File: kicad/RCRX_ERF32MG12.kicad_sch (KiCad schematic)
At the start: 79 parts, among them J21 BUZZER, J22 USB_OTG, P1 Nokia 5110 display, Q1 Q_PMOS_DGS, SW1 RESET, U1 PIC16(L)F1459-I_ML

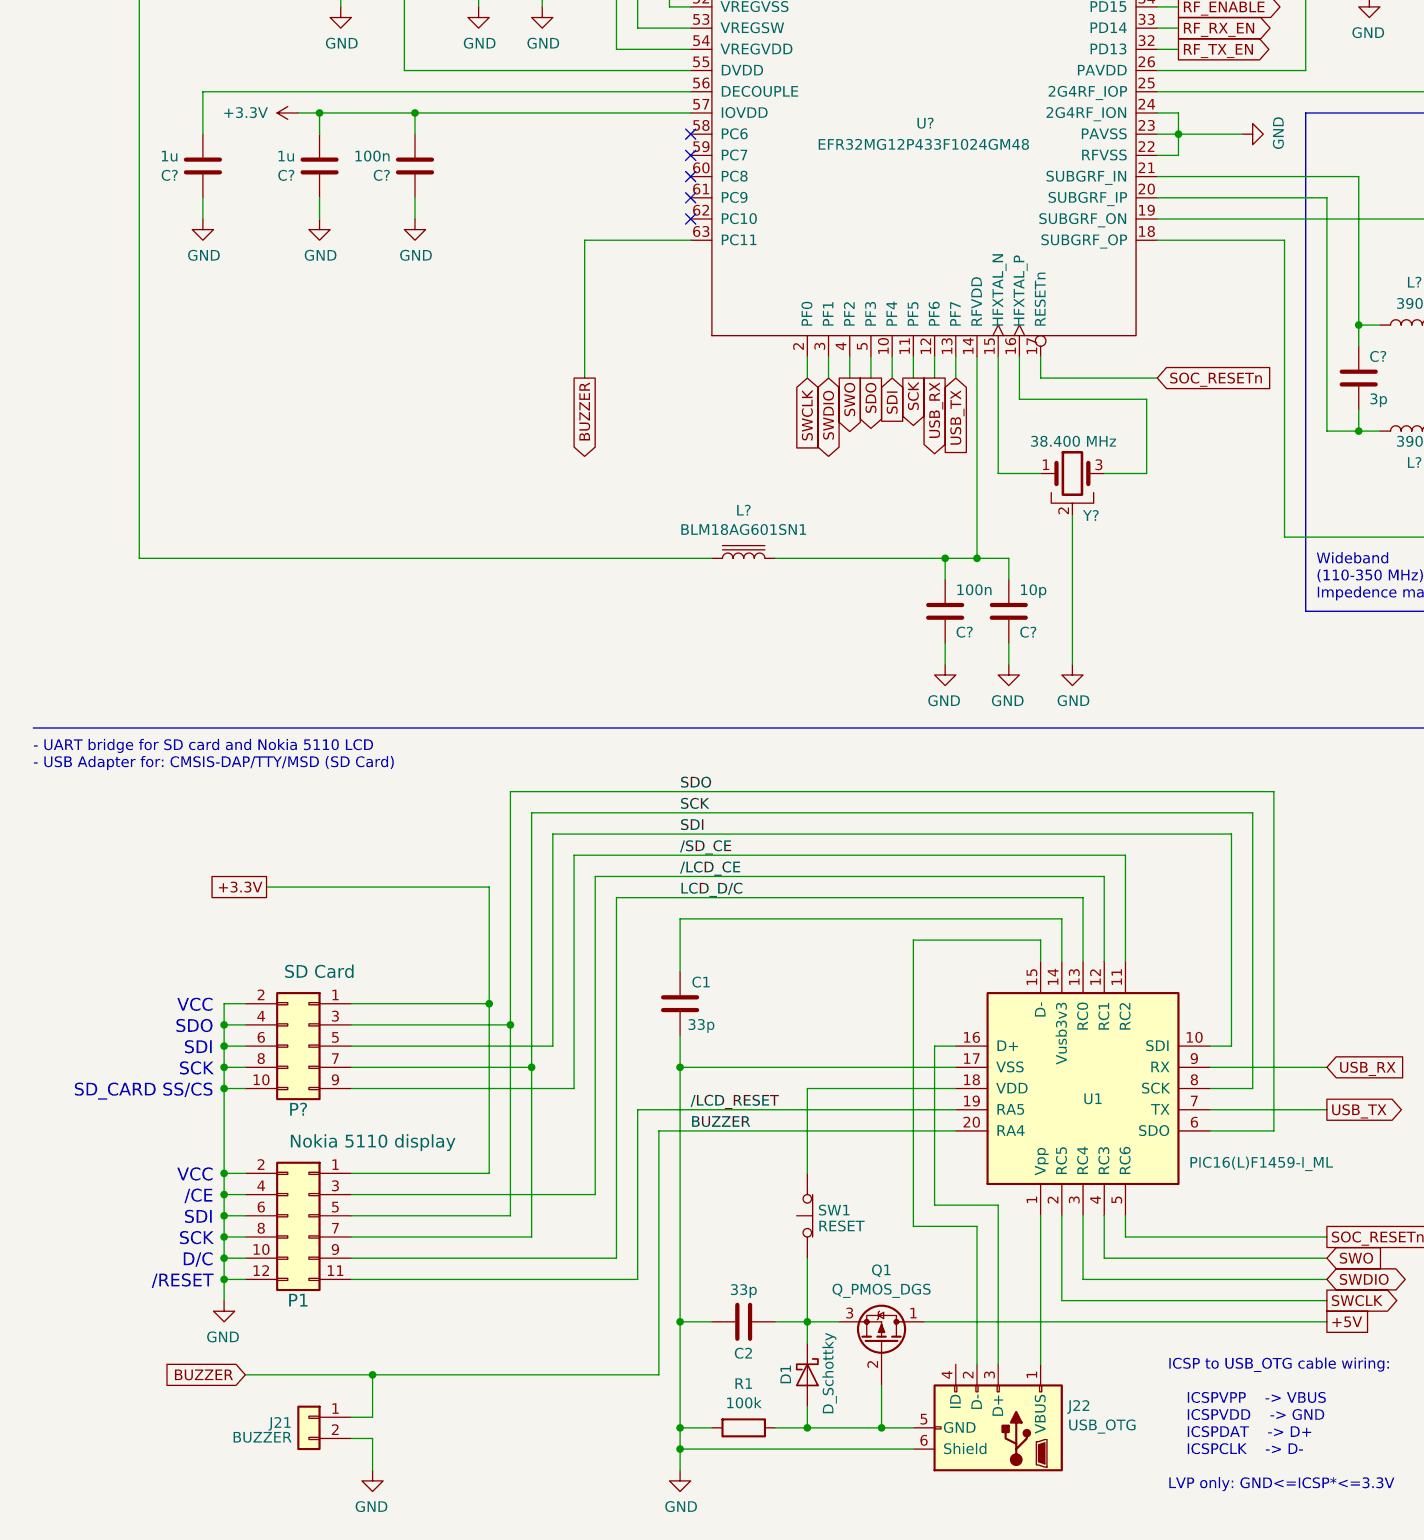
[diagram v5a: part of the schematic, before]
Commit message: Changing the buzzer connector
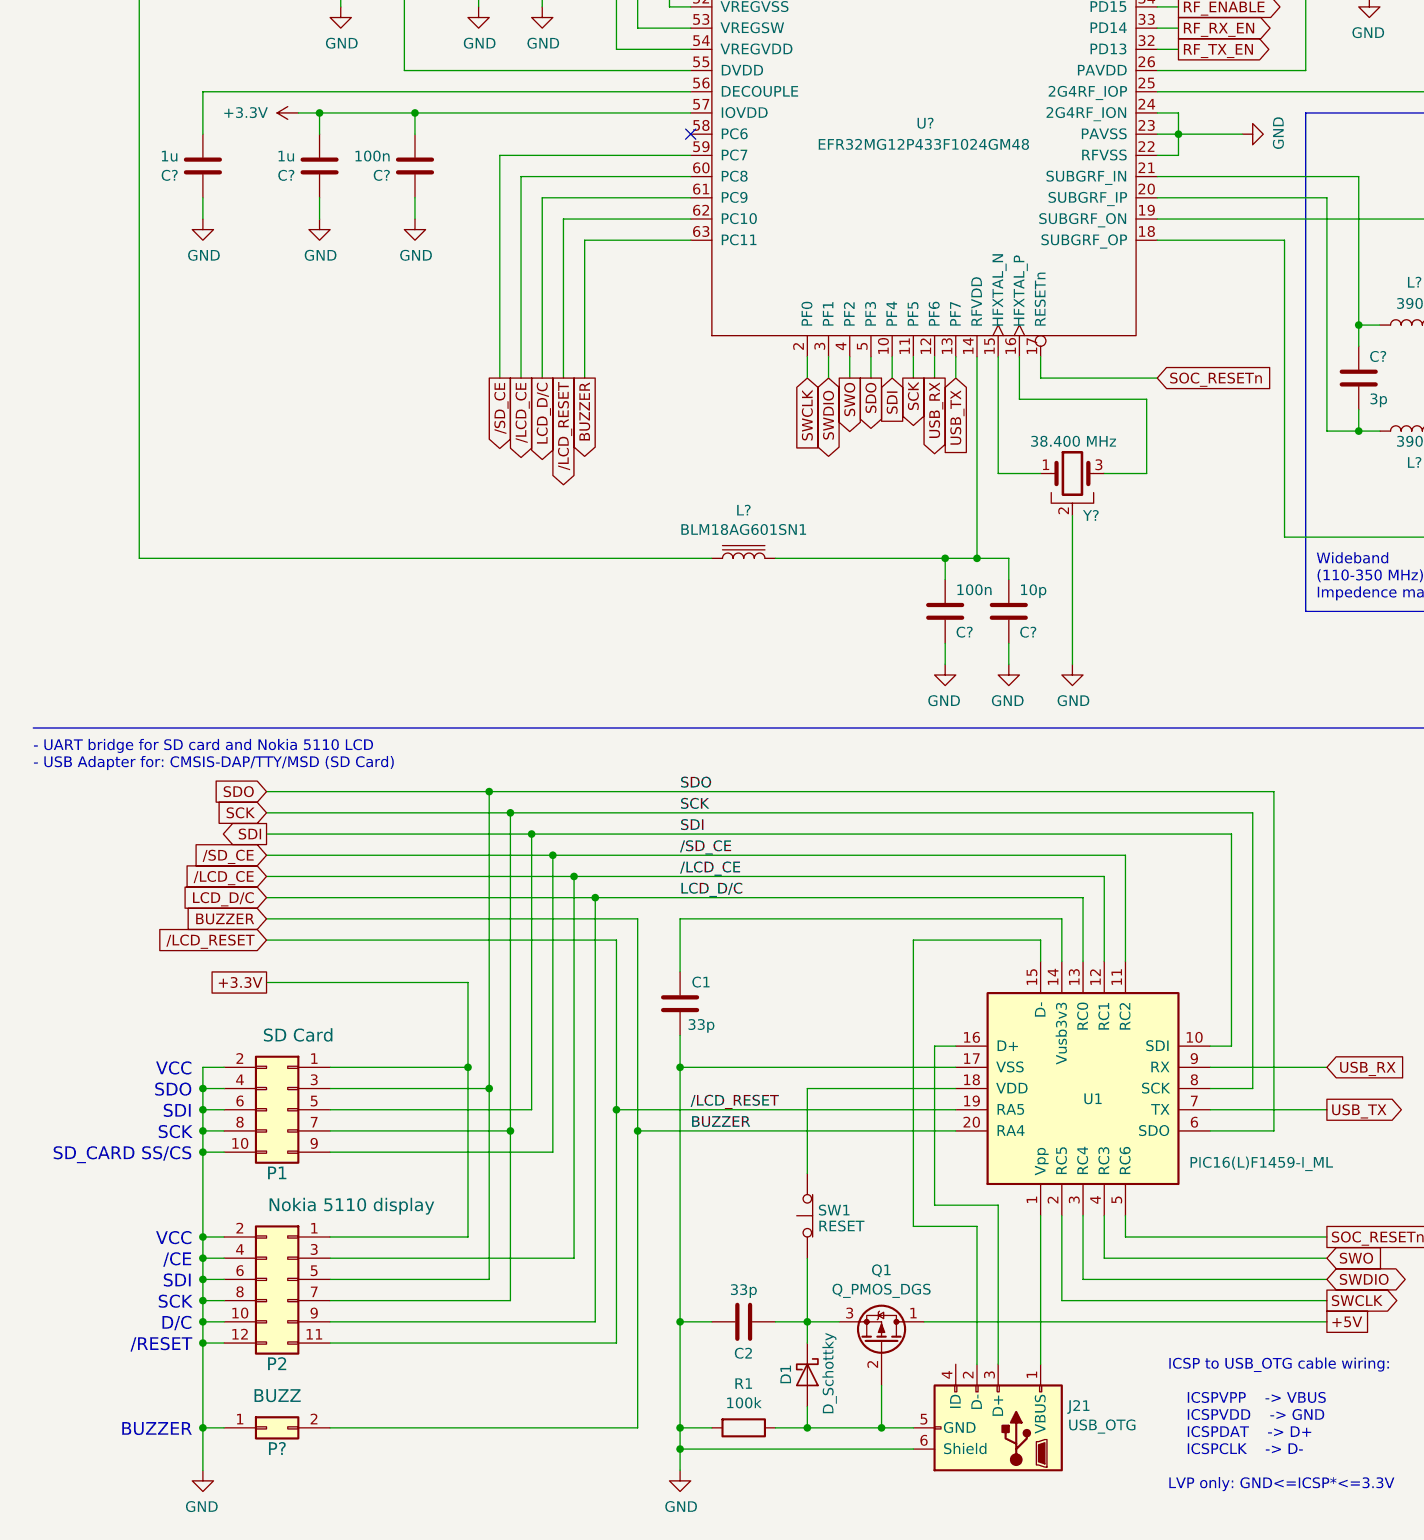
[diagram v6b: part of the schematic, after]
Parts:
- removed J21: BUZZER, symbol Connector_Generic:Conn_01x02
- removed J22: USB_OTG, symbol conn:USB_OTG
- removed P1: Nokia 5110 display, symbol conn:Conn_02x06_Odd_Even
- removed P?: SD Card, symbol conn:Conn_02x05_Odd_Even
- added J21: USB_OTG, symbol conn:USB_OTG
- added P1: SD Card, symbol conn:Conn_02x05_Odd_Even
- added P2: Nokia 5110 display, symbol conn:Conn_02x06_Odd_Even
- added P?: BUZZ, symbol conn:Conn_02x01
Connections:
- net +3V3: now also P1.1 (Pin_1), P2.1 (Pin_1)
- net BUZZER: now also P?.2 (Pin_2)
- net GND: now also J21.6 (Shield), P1.10 (Pin_10), P1.2 (Pin_2), P1.4 (Pin_4), P1.6 (Pin_6), P1.8 (Pin_8), P2.10 (Pin_10), P2.12 (Pin_12), P2.2 (Pin_2), P2.4 (Pin_4), P2.6 (Pin_6), P2.8 (Pin_8), P?.1 (Pin_1)
- net LCD_D/C: now also U?.61 (PC9), P2.9 (Pin_9)
- net SCK: now also P1.7 (Pin_7), P2.7 (Pin_7)
- net SDI: now also P1.5 (Pin_5)
- net SDO: now also P1.3 (Pin_3), P2.5 (Pin_5)
- net /LCD_CE: now also U?.60 (PC8), P2.3 (Pin_3)
- net /LCD_RESET: now also U?.62 (PC10), P2.11 (Pin_11)
- net /SD_CE: now also U?.59 (PC7), P1.9 (Pin_9)
- net at D1.2 (A), Q1.2 (G), R1.1: now also J21.5 (GND)
- net at U1.1 (Vpp): now also J21.1 (VBUS)
- net at U1.15 (D-): now also J21.2 (D-)
- net at U1.16 (D+): now also J21.3 (D+)
- no-connect marks 8 -> 4
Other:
- note added: "BUZZER"

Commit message: Using SAMD11D14M instead of PIC16F1459 for USB bridge - updating schematics
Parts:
- removed C1, C2: 33p, symbol device:C
- removed D1: D_Schottky, symbol device:D_Schottky
- removed J21: USB_OTG, symbol conn:USB_OTG
- removed P1: SD Card, symbol conn:Conn_02x05_Odd_Even
- removed P2: Nokia 5110 display, symbol conn:Conn_02x06_Odd_Even
- removed P?: BUZZ, symbol conn:Conn_02x01
- removed Q1: Q_PMOS_DGS, symbol device:Q_PMOS_DGS
- removed R1: 100k, symbol device:R
- removed SW1: RESET, symbol switches:SW_Push_Open
- removed U1: PIC16(L)F1459-I_ML, symbol PIC_USB_BRIDGE:PIC16(L)F1459-I_ML
- added C16: 100n, symbol device:C
- added C17, C19: 4.7u, symbol device:C
- added J20: USB_OTG, symbol conn:USB_OTG
- added J21, J22: USB, symbol Connector_Generic:Conn_01x03
- added P10: LEDs, symbol conn:Conn_02x06_Odd_Even
- added P6: SD Card, symbol conn:Conn_02x05_Odd_Even
- added P9: BUZZ, symbol conn:Conn_02x01
- added P?: DAP, symbol Connector_Generic:Conn_02x09_Odd_Even
- added P?: Nokia 5110 display, symbol Connector_Generic:Conn_02x07_Odd_Even
- added R10: 1M, symbol device:R
- added R7: 1k, symbol device:R
- added U10: ATSAMD11D14A-M, Package_DFN_QFN:QFN-24-1EP_4x4mm_P0.5mm_EP2.6x2.6mm, symbol MCU_Microchip_SAMD:ATSAMD11D14A-M
- added U11: USB6B1, Package_SO:SOIC-8_3.9x4.9mm_P1.27mm, symbol Power_Protection:USB6B1
- C?: value 100n -> 2.0pF
- C?: value 100n -> 1.0pF
- L?: value L -> 1.8nH
- L?: value L -> 3.0nH
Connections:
- net +3V3: now also C16.2, C17.2, P10.3 (Pin_3), P6.1 (Pin_1), P?.1 (Pin_1), P?.3 (Pin_3), R7.2, U10.24 (VDD)
- net +5V: now also P10.1 (Pin_1), P?.1 (Pin_1)
- net GND: now also C16.1, C17.1, C19.1, J20.5 (GND), J21.3 (Pin_3), J22.3 (Pin_3), P10.10 (Pin_10), P10.12 (Pin_12), P10.2 (Pin_2), P10.4 (Pin_4), P10.6 (Pin_6), P10.8 (Pin_8), P6.10 (Pin_10), P6.2 (Pin_2), P6.4 (Pin_4), P6.6 (Pin_6), P6.8 (Pin_8), P9.2 (Pin_2), P?.10 (Pin_10), P?.10 (Pin_10), P?.12 (Pin_12), P?.12 (Pin_12), P?.14 (Pin_14), P?.14 (Pin_14), P?.16 (Pin_16), P?.18 (Pin_18), P?.2 (Pin_2), P?.2 (Pin_2), P?.4 (Pin_4), P?.4 (Pin_4), P?.6 (Pin_6), P?.6 (Pin_6), P?.8 (Pin_8), P?.8 (Pin_8), R10.1, U10.23 (GND)
- net SOC_RESETn: now also P?.5 (Pin_5), U10.5 (PA06)
- net USB_RX: now also U10.3 (PA04)
- net USB_TX: now also U10.4 (PA05)
- net BUZZER: no longer names the net of U?.63 (PC11)
- net LCD_D/C: no longer names the net of U?.61 (PC9)
- net SCK: no longer names the net of U?.11 (PF5)
- net SDI: no longer names the net of U?.10 (PF4)
- net SDO: no longer names the net of U?.5 (PF3)
- net SWCLK renamed SOC_SWCLK
- net SOC_SWCLK: now also P?.11 (Pin_11), U10.8 (PA09)
- net SWDIO renamed SOC_SWDIO
- net SOC_SWDIO: now also P?.9 (Pin_9), U10.7 (PA08)
- net SWO renamed SOC_SWO
- net SOC_SWO: now also P?.7 (Pin_7), U10.6 (PA07)
- net /LCD_CE: no longer names the net of U?.60 (PC8)
- net /LCD_RESET: no longer names the net of U?.62 (PC10)
- net /SD_CE: no longer names the net of U?.59 (PC7)
- new net: J21.1 (Pin_1), U10.21 (PA24/D-)
- new net: J21.2 (Pin_2), U10.22 (PA25/D+)
- new net: J20.1 (VBUS), U11.1 (VBUS), U11.8 (VBUS)
- new net: J22.1 (Pin_1), U11.2 (I/O1)
- new net: J22.2 (Pin_2), U11.3 (I/O2)
- new net: C19.2, J20.6 (Shield), R10.2, U11.4 (GND), U11.5 (GND)
- new net: J20.2 (D-), U11.6 (I/O2)
- new net: J20.3 (D+), U11.7 (I/O1)
- new net: P9.1 (Pin_1), U10.15 (PA22)
- new net: P6.3 (Pin_3), U10.9 (PA10)
- new net: P10.5 (Pin_5), P6.5 (Pin_5), P?.5 (Pin_5), U10.11 (PA14)
- new net: P10.7 (Pin_7), P6.7 (Pin_7), P?.7 (Pin_7), U10.10 (PA11)
- new net: P6.9 (Pin_9), U10.1 (PA02)
- new net: P?.9 (Pin_9), U10.12 (PA15)
- new net: P?.11 (Pin_11), U10.13 (PA16)
- new net: P?.13 (Pin_13), U10.14 (PA17)
- new net: P10.9 (Pin_9), U10.16 (PA23)
- new net: P10.11 (Pin_11), U10.17 (PA27)
- new net: P?.3 (Pin_3), U10.2 (PA03)
- new net DAP_RESETn: P?.17 (Pin_17), U10.18 (PA28/~{RST})
- new net DAP_SWCLK: P?.15 (Pin_15), R7.1, U10.19 (PA30/SWCLK)
- new net DAP_SWDIO: P?.13 (Pin_13), U10.20 (PA31/SWDIO)
- no-connect marks 4 -> 13
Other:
- note added: "- Micro USB connector"
- note added: "- UART bridge for SD card, Nokia 5110 LCD, LEDs and BUZZER - USB Adapter for: CMSIS-DAP/TTY/MSD (SD Card)"
- note added: "/CS"
- note added: "BL_PWM"
- note added: "LE"
- note added: "MISO"
- note added: "MOSI"
- note added: "PWM"
- note added: "SCLK"
- note added: "VLED"
- note added: "an930.1-efr32-series-1.pdf Rev.05 page 27 C: GRM1555 SMD L: LQP15MN film type"
- note removed: "- UART bridge for SD card and Nokia 5110 LCD - USB Adapter for: CMSIS-DAP/TTY/MSD (SD Card)"
- note removed: "2.4 GHz band filter"
- note removed: "BUZZER"
- note removed: "ICSP to USB_OTG cable wiring: ICSPVPP -> VBUS ICSPVDD -> GND ICSPDAT -> D+ ICSPCLK -> D- LVP only: GND<=ICSP*<=3.3V"
- note removed: "SCK"
- note removed: "SDI"
- note removed: "SDO"
- note removed: "SD_CARD SS/CS"

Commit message: Driving the EFR32 reset with the SAMD11 reset pin as GPIO to have an additional GPIO for the SPI {EFR32<->SAMD11} CLK
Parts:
- removed C? (x2): 100n, symbol device:C
- removed C? (x2): 4u7, symbol device:CP
- removed C? (x4): 1u, symbol device:C
- removed C?: 2.0pF, symbol device:C
- removed C?: 1.0pF, symbol device:C
- removed C? (x6): 100p, symbol device:C
- removed J?: 50 Ohm 430-460 MHz Antenna, symbol conn:Conn_Coaxial
- removed J?: 50 Ohm 13-79 MHz Antenna, symbol conn:Conn_Coaxial
- removed J?: 50 Ohm 2.4 GHz Antenna, symbol conn:Conn_Coaxial
- removed L?: 1.8nH, symbol device:L
- removed L?: 3.0nH, symbol device:L
- removed P?: BATT, symbol conn:Conn_01x03
- removed P?: Nokia 5110 display, symbol Connector_Generic:Conn_02x07_Odd_Even
- removed U?: LM1117-5.0, symbol regul:LM1117-5.0
- removed U?: LM1117-3.3, symbol regul:LM1117-5.0
- removed U? (x2): TLV70245_SOT23-5, TO_SOT_Packages_SMD:SOT-23-5, symbol regul:TLV70245_SOT23-5
- removed U? (x2): MAX2650, smd-semi:SOT-143, symbol maxim_1:MAX2650
- removed U?: ADE-1+, RF_Mini-Circuits:Mini-Circuits_CD542_LandPatternPL-052, symbol RF_Mixer:ADE-1+
- removed U?: RLP-83+, symbol RF:RLP-83+
- removed U?: RBP-440+, symbol RF:RBP-440+
- removed Y?: 514CCAXXXXXXCAG, Si500D, symbol Si500D:Si514
- added C1, C18, C2, C20, C21, C22: 100p, symbol device:C
- added C23, C? (x2): 100n, symbol device:C
- added C? (x2): 4u7, symbol device:CP
- added C? (x4): 1u, symbol device:C
- added C?: 2.0pF, symbol device:C
- added C?: 1.0pF, symbol device:C
- added J?: 50 Ohm 13-79 MHz Antenna, symbol conn:Conn_Coaxial
- added J?: 50 Ohm 2.4 GHz Antenna, symbol conn:Conn_Coaxial
- added J?: 50 Ohm 433-460 MHz Antenna, symbol conn:Conn_Coaxial
- added L?: 1.8nH, symbol device:L
- added L?: 3.0nH, symbol device:L
- added P?: POWER_IN, Connectors_Samtec:SL-104-X-XX_1x04, symbol RCTX-rescue:Conn_01x04-conn
- added P?: Nokia 5110 display, symbol Connector_Generic:Conn_02x07_Odd_Even
- added R1: 10k, symbol device:R
- added R8: 330, symbol device:R
- added R?: 10, symbol device:R
- added RV?: POT, Potentiometers:Potentiometer_Trimmer_ACP_CA6v_Horizontal, symbol RCTX-rescue:POT_TRIM-device
- added SW1: SW_Push-switches, symbol RCTX-rescue:SW_Push-switches
- added U1, U12: MAX2650, smd-semi:SOT-143, symbol maxim_1:MAX2650
- added U?: RLP-83+, symbol RF:RLP-83+
- added U?: LM1117-5.0, symbol regul:LM1117-5.0
- added U?: LM1117-3.3, symbol regul:LM1117-5.0
- added U?: ADE-1+, RF_Mini-Circuits:Mini-Circuits_CD542_LandPatternPL-052, symbol RF_Mixer:ADE-1+
- added U? (x2): TLV70245_SOT23-5, TO_SOT_Packages_SMD:SOT-23-5, symbol regul:TLV70245_SOT23-5
- added U?: RBP-440+, symbol RF:RBP-440+
- added Y?: 514CCAXXXXXXCAG, Si500D, symbol Si500D:Si514
- added ZD?: ZENER, Diodes_THT:D_5W_P5.08mm_Vertical_KathodeUp, symbol RCTX-rescue:D_Zener-device
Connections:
- net RF_ENABLE is gone; now on an unnamed net: U?.34 (AVDD)
- net +3V3: now also U?.39 (VREGVDD), U?.42 (IOVDD), C?.1, C?.1, P?.1 (Pin_1), R1.2, U?.2 (VO), Y?.6 (VDD); no longer U?.54 (VREGVDD), U?.57 (IOVDD)
- net +5V: now also C?.1, C?.1, U?.2 (VO)
- net CRSF_RX: now also U?.35 (PB14); no longer U?.50 (PB14)
- net CRSF_TX: now also U?.36 (PB15); no longer U?.51 (PB15)
- net DAP_RESETn: now also R8.1, SW1.2; no longer U10.18 (PA28/~{RST})
- net GND: now also U?.17 (RFVSS), U?.18 (VSS), U?.19 (2G4RF_ION), U?.37 (VREGVSS), C18.2, C20.2, C23.1, C?.1, C?.1, C?.2, C?.2, C?.2, C?.2, C?.2, C?.2, C?.2, C?.2, J?.2 (Ext), J?.2 (Ext), J?.2 (Ext), P?.10 (Pin_10), P?.12 (Pin_12), P?.14 (Pin_14), P?.2 (Pin_2), P?.2 (Pin_2), P?.3 (Pin_3), P?.4 (Pin_4), P?.6 (Pin_6), P?.8 (Pin_8), SW1.1, U1.4 (VCC), U12.2 (GND), U?.1 (GND), U?.1 (GND), U?.1 (GND), U?.1 (GND), U?.1 (LO1), U?.2 (GND), U?.2 (GND), U?.2 (GND), U?.2 (GND), U?.3 (GND), U?.3 (GND), U?.4 (IF2), U?.5 (GND), U?.5 (GND), U?.5 (RF2), U?.6 (GND), U?.6 (GND), U?.7 (GND), U?.7 (GND), Y?.3 (GND); no longer U?.0 (VSS), U?.22 (RFVSS), U?.23 (PAVSS), U?.24 (2G4RF_ION), U?.52 (VREGVSS)
- net I2C_SCL: now also U?.32 (PB12); no longer U?.47 (PB12)
- net I2C_SDA: now also U?.31 (PB11); no longer U?.46 (PB11)
- net RF_RX_EN: now also U?.23 (PD14), U?.3 (EN); no longer U?.33 (PD14)
- net RF_RX_VCC: now also C20.1, C?.1, U12.4 (VCC), U?.5 (OUT)
- net RF_TX_EN: now also U?.22 (PD13), U?.3 (EN); no longer U?.32 (PD13)
- net RF_TX_VCC: now also C18.1, C?.1, U1.2 (GND), U?.5 (OUT)
- net SOC_RESETn: now also U10.18 (PA28/~{RST}), U?.12 (RESETn), C23.2, R1.1, R8.2; no longer U10.5 (PA06), U?.17 (RESETn)
- net SOC_SWCLK: now also U?.1 (PF0); no longer U?.2 (PF0)
- net SOC_SWDIO: now also U?.2 (PF1); no longer U?.3 (PF1)
- net SOC_SWO: now also U?.3 (PF2); no longer U?.4 (PF2)
- net VDCDC: now also U?.40 (DVDD); no longer U?.55 (DVDD)
- net at U?.10 (HFXTAL_N): now also Y?.1
- net at U?.11 (HFXTAL_P): now also Y?.3
- net at C?.2, C?.2, L?.1: now also U?.9 (RFVDD); no longer U?.14 (RFVDD)
- net at U?.15 (SUBGRF_IP): now also C?.2, L?.1; no longer Y?.1
- net at U?.16 (SUBGRF_IN): now also C?.1, L?.1; no longer Y?.3
- net at C?.2, C?.2, L?.2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: now also U?.13 (SUBGRF_OP); no longer U?.18 (SUBGRF_OP)
- net at C?.1, C?.1, L?.1: now also U?.14 (SUBGRF_ON); no longer U?.19 (SUBGRF_ON)
- net at U?.25 (PA0): now also HEX_SW?.1 (CM)
- net at C?.2, C?.2, L?.1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: now also U?.21 (PAVDD); no longer U?.26 (PAVDD)
- net at HEX_SW?.1 (CM): now also U?.26 (PA1); no longer U?.36 (PA1)
- net at HEX_SW?.2 (D0), HEX_SW?.2 (D0): now also U?.27 (PA2); no longer U?.37 (PA2)
- net at HEX_SW?.3 (D1), HEX_SW?.3 (D1): now also U?.28 (PA3); no longer U?.38 (PA3)
- net at HEX_SW?.4 (D2), HEX_SW?.4 (D2): now also U?.29 (PA4); no longer U?.39 (PA4)
- net at HEX_SW?.5 (D3), HEX_SW?.5 (D3): now also U?.30 (PA5); no longer U?.40 (PA5)
- net at C?.1, C?.1, R?.1: no longer U?.49 (AVDD)
- net at L?.2: now also U?.38 (VREGSW); no longer U?.53 (VREGSW)
- net at C?.1: now also U?.41 (DECOUPLE); no longer U?.56 (DECOUPLE)
- net at C?.2, L?.1: now also U?.2 (IF1)
- net at P10.5 (Pin_5), P6.5 (Pin_5), U10.11 (PA14): now also P?.5 (Pin_5)
- net at P10.7 (Pin_7), P6.7 (Pin_7), U10.10 (PA11): now also P?.7 (Pin_7)
- net at U10.12 (PA15): now also P?.9 (Pin_9)
- net at U10.13 (PA16): now also P?.11 (Pin_11)
- net at U10.14 (PA17): now also P?.13 (Pin_13)
- net at U10.2 (PA03): now also P?.3 (Pin_3)
- net USB_RX renamed SPI_MISO
- net SPI_MISO: now also U?.8 (PF7); no longer U?.12 (PF6)
- net USB_TX renamed SPI_MOSI
- net SPI_MOSI: now also U?.7 (PF6); no longer U?.13 (PF7)
- new net: L?.2, U?.20 (2G4RF_IOP)
- new net: R?.1, Y?.4 (CLK+)
- new net: R?.2, U?.6 (LO2)
- new net: C22.2, U12.1 (OUT)
- new net: C2.1, U12.3 (IN)
- new net: J?.1 (In), U?.4 (RF) (x2)
- new net: C?.2, L?.1, L?.2
- new net: C21.2, C22.1, U?.8 (RF), U?.8 (RF)
- new net: C1.1, C2.2, U?.3 (RF1)
- new net: C?.2, J?.1 (In), L?.1
- new net: RV?.2, RV?.3, ZD?.1 (K)
- new net: C1.2, U1.1 (OUT)
- new net: C21.1, U1.3 (IN)
- new net: P?.4 (Pin_4), ZD?.2 (A)
- new net +BATT: C?.1, C?.1, P?.1 (Pin_1), RV?.1, U?.1 (IN), U?.1 (IN), U?.3 (VI), U?.3 (VI)
- new net SCL: Y?.2 (SCL)
- new net SDA: Y?.1 (SDA)
- new net SPI_SCK: U10.5 (PA06), U?.6 (PF5)
- no-connect marks 13 -> 11
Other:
- note added: "AMPEROMETER"
- note added: "Main power source"
- moved on the sheet: C?, HEX_SW?, L?, P?, R?, U?, Y?
